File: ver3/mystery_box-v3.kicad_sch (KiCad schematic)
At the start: 3 parts, among them J1 Conn_01x02_Socket, Q1 IRLZ44N

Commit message: first draft v3
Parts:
- added D1, D2, D3: D, symbol Device:D
- added J2, J3, J4, J5: Conn_01x02_Socket, symbol Connector:Conn_01x02_Socket
- added Q2, Q3: IRLZ44N, Package_TO_SOT_THT:TO-220-3_Vertical, symbol Transistor_FET:IRLZ44N
- added R1, R2: R, symbol Device:R
- added U1: TXS0102DQE, Package_SON:X2SON-8_1.4x1mm_P0.35mm, symbol Logic_LevelTranslator:TXS0102DQE
- added U2: MAX485E, Package_SO:SOIC-8_3.9x4.9mm_P1.27mm, symbol Interface_UART:MAX485E
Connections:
- net GND: now also ESP32_S1. (14), Q2.3 (S), Q3.3 (S)
- net VCC 12V: now also D1.1 (K), D2.1 (K), D3.1 (K), J2.1 (Pin_1), J3.1 (Pin_1)
- net at J1.2 (Pin_2), Q1.2 (D): now also D1.2 (A)
- new net: D3.2 (A), J3.2 (Pin_2), Q3.2 (D)
- new net: J4.1 (Pin_1), R2.1
- new net: R2.2, U1.3 (A2)
- new net: J4.2 (Pin_2), R1.1
- new net: R1.2, U1.2 (A1)
- new net: ESP32_S1. (14), Q2.1 (G)
- new net: ESP32_S1. (14), Q3.1 (G)
- new net: ESP32_S1. (14), U1.6 (B2)
- new net: ESP32_S1. (14), U1.7 (B1)
- new net: ESP32_S1. (14), U2.3 (DE)
- new net: ESP32_S1. (14), U2.4 (DI)
- new net: D2.2 (A), J2.2 (Pin_2), Q2.2 (D)
- new net: J5.1 (Pin_1), U2.6 (A)
- new net: J5.2 (Pin_2), U2.7 (B)
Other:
- moved on the sheet: ESP32_S1, J1, Q1

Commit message: update 2. meeting
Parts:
- removed J1, J2, J3, J4, J5: Conn_01x02_Socket, symbol Connector:Conn_01x02_Socket
- removed U1: TXS0102DQE, Package_SON:X2SON-8_1.4x1mm_P0.35mm, symbol Logic_LevelTranslator:TXS0102DQE
- added F1, F2, F3, F4: Fuse, symbol Device:Fuse
- added J1, J10, J11, J12, J13, J14, J15, J16, J17, J2, J3, J4, J5, J7, J8, J9: Screw_Terminal_01x02, symbol Connector:Screw_Terminal_01x02
- added J18: RJ45 POE, symbol Connector:RJ45
- added J19: RJ45 IN, symbol Connector:RJ45
- added J6: Conn_01x02_Socket, symbol Connector:Conn_01x02_Socket
- added R10, R3, R6, R8: 100K, symbol Device:R
- added R4, R5, R7, R9: 330K, symbol Device:R
- added U1: ~, eigene_footprints:level_shifter, symbol eigene:levelshifter_2channel
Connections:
- net GND: now also U2.5 (GND), J10.1 (Pin_1), J11.1 (Pin_1), J12.1 (Pin_1), J13.1 (Pin_1), J14.1 (Pin_1), J15.1 (Pin_1), J16.1 (Pin_1), J17.1 (Pin_1), J18.7, J18.8, J6.1 (Pin_1), J7.1 (Pin_1), J8.1 (Pin_1), J9.1 (Pin_1), R10.1, R3.1, R6.1, R8.1, U1.10 (GND), U1.4 (GND)
- net VCC 12V: now also F1.2, F2.1, F3.1, F4.1, J18.4, J18.5, J6.2 (Pin_2), J7.2 (Pin_2); no longer D1.1 (K), D2.1 (K), D3.1 (K)
- net at D3.2 (A), Q3.2 (D): now also J2.2 (Pin_2)
- net at R2.1: now also J5.1 (Pin_1)
- net at R2.2: now also U1.7 (HV1)
- net at R1.1: now also J5.2 (Pin_2)
- net at R1.2: now also U1.11 (HV3)
- net at D1.2 (A), Q1.2 (D): now also J1.2 (Pin_2)
- net at D2.2 (A), Q2.2 (D): now also J3.2 (Pin_2)
- net at U2.6 (A): now also J4.1 (Pin_1)
- net at U2.7 (B): now also J4.2 (Pin_2)
- net VCC 5V: now reaches U2.8 (VCC)
- net VCC 5V: now also U1.9 (HV)
- new net: ESP32_S1. (14), R7.1, R8.2
- new net: D2.1 (K), F2.2, J3.1 (Pin_1), R7.2
- new net: ESP32_S1. (14), R10.2, R9.1
- new net: F1.1, J10.2 (Pin_2), J11.2 (Pin_2), J12.2 (Pin_2), J13.2 (Pin_2), J14.2 (Pin_2), J15.2 (Pin_2), J16.2 (Pin_2), J17.2 (Pin_2), J8.2 (Pin_2), J9.2 (Pin_2), R4.2
- new net: J18.1, J19.1
- new net: J18.2, J19.2
- new net: J18.3, J19.3
- new net: J18.6, J19.6
- new net: D1.1 (K), F4.2, J1.1 (Pin_1), R5.2
- new net: D3.1 (K), F3.2, J2.1 (Pin_1), R9.2
- new net: ESP32_S1. (14), R5.1, R6.2
- new net: ESP32_S1. (14), U1.1 (LV1)
- new net: ESP32_S1. (14), U1.5 (LV3)
- new net: ESP32_S1. (14), R3.2, R4.1
- new net VCC 3V3: U1.3 (LV)
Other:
- moved on the sheet: D1, D2, Q1, Q2, R1, R2, U2

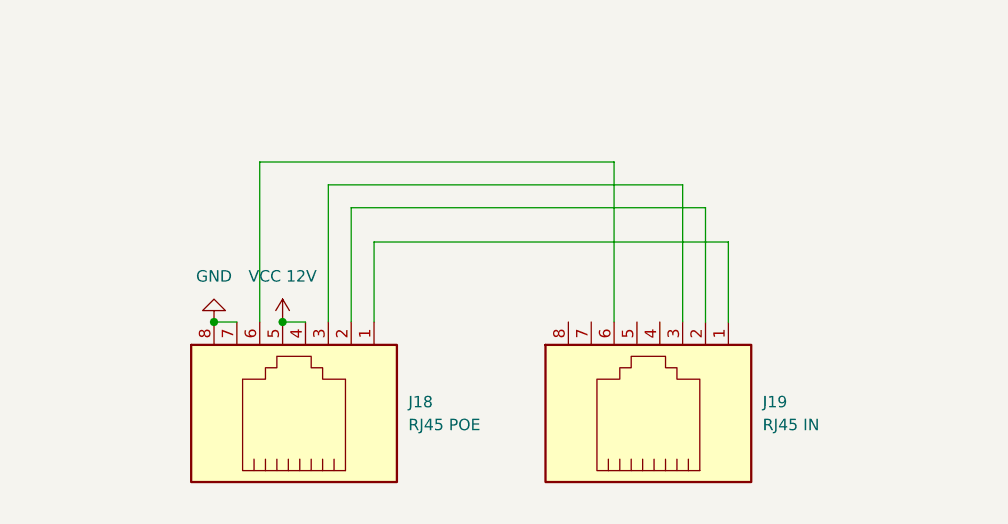
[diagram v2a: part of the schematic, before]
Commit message: added footprints for rj45, max485 module
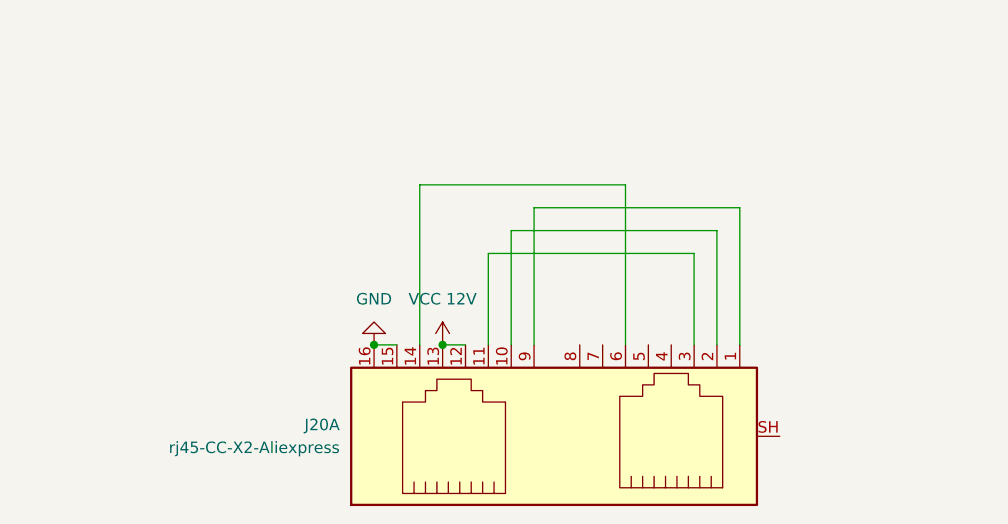
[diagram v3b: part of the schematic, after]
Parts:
- removed J18: RJ45 POE, symbol Connector:RJ45
- removed J19: RJ45 IN, symbol Connector:RJ45
- added J20: rj45-CC-X2-Aliexpress, eigene_footprints:RJ45_X2_CC_Aliexpress, symbol eigene:rj45-CC-X2-Aliexpress
- R1: footprint (none) -> Resistor_THT:R_Axial_DIN0207_L6.3mm_D2.5mm_P10.16mm_Horizontal
- U2: footprint Package_SO:SOIC-8_3.9x4.9mm_P1.27mm -> eigene_footprints:max845 modul
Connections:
- net GND: now also J20.15, J20.16
- net VCC 12V: now also J20.12, J20.13
- new net: J20.1, J20.9
- new net: J20.10, J20.2
- new net: J20.11, J20.3
- new net: J20.14, J20.6

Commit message: pcb editor beginning
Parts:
- removed ESP32_S1: ~, symbol waveshare_esp32_s3_mini_zero:Waveshare_ESP32_S3_Mini_Zero
- removed J4: Screw_Terminal_01x02, symbol Connector:Screw_Terminal_01x02
- removed J6: Conn_01x02_Socket, symbol Connector:Conn_01x02_Socket
- added ESP32_S1: ~, eigene_footprints:ESP32-S3-Zero, symbol eigene:Waveshare_ESP32_S3_Mini_Zero
- added J18: Barrel_Jack_MountingPin, eigene_footprints:CUI_PJ-050BH, symbol Connector:Barrel_Jack_MountingPin
- added dmx_out1: DMX Out, TerminalBlock:TerminalBlock_MaiXu_MX126-5.0-03P_1x03_P5.00mm, symbol Connector:Screw_Terminal_01x03
- 12v_input_terminal1: renamed from J7; footprint (none) -> TerminalBlock:TerminalBlock_MaiXu_MX126-5.0-02P_1x02_P5.00mm
- D1, D2, D3: footprint (none) -> Diode_THT:D_DO-15_P10.16mm_Horizontal
- F1, F2, F3, F4: footprint (none) -> eigene_footprints:FUSE SPACIGER SPACER
- J10, J11, J12, J13, J14, J15, J16, J17, J8, J9: footprint (none) -> TerminalBlock:TerminalBlock_MaiXu_MX126-5.0-02P_1x02_P5.00mm
- R10, R2, R3, R4, R5, R6, R7, R8, R9: footprint (none) -> Resistor_THT:R_Axial_DIN0207_L6.3mm_D2.5mm_P10.16mm_Horizontal
- neopixel_out1: renamed from J5; footprint (none) -> TerminalBlock:TerminalBlock_MaiXu_MX126-5.0-02P_1x02_P5.00mm
- switched_output_01: renamed from J3; footprint (none) -> TerminalBlock:TerminalBlock_MaiXu_MX126-5.0-02P_1x02_P5.00mm
- switched_output_02: renamed from J1; footprint (none) -> TerminalBlock:TerminalBlock_MaiXu_MX126-5.0-02P_1x02_P5.00mm
- switched_output_03: renamed from J2; footprint (none) -> TerminalBlock:TerminalBlock_MaiXu_MX126-5.0-02P_1x02_P5.00mm
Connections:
- net GND: now also ESP32_S1. (7), J18.2, dmx_out1.1 (Pin_1)
- net VCC 12V: now also J18.1
- net at R7.1, R8.2: now also ESP32_S1. (7)
- net at R2.1: now also neopixel_out1.2 (Pin_2); no longer neopixel_out1.1 (Pin_1)
- net at R10.2, R9.1: now also ESP32_S1. (7)
- net at R1.1: now also neopixel_out1.1 (Pin_1); no longer neopixel_out1.2 (Pin_2)
- net at Q1.1 (G): now also ESP32_S1. (7)
- net at Q2.1 (G): now also ESP32_S1. (7)
- net at R5.1, R6.2: now also ESP32_S1. (7)
- net at Q3.1 (G): now also ESP32_S1. (7)
- net at U1.1 (LV1): now also ESP32_S1. (7)
- net at U1.5 (LV3): now also ESP32_S1. (7)
- net at R3.2, R4.1: now also ESP32_S1. (7)
- net at U2.3 (DE): now also ESP32_S1. (7)
- net at U2.4 (DI): now also ESP32_S1. (7)
- net at U2.6 (A): now also dmx_out1.2 (Pin_2)
- net at U2.7 (B): now also dmx_out1.3 (Pin_3)
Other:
- moved on the sheet: neopixel_out1

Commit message: smart switch
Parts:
- removed F1, F2, F3, F4: Fuse, eigene_footprints:FUSE SPACIGER SPACER, symbol Device:Fuse
- removed R10, R6, R8: 100K, Resistor_THT:R_Axial_DIN0207_L6.3mm_D2.5mm_P10.16mm_Horizontal, symbol Device:R
- removed R4, R5, R7, R9: 330K, Resistor_THT:R_Axial_DIN0207_L6.3mm_D2.5mm_P10.16mm_Horizontal, symbol Device:R
- added U3: ~, Package_SO:SOIC-8_3.9x4.9mm_P1.27mm, symbol eigene:BV1HD090FJ-C
- R3: value 100K -> R100K
- renumbered ESP32_S1 to ESP32_S3
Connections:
- net GND: now also U3.3 (GND); no longer R3.1
- net VCC 12V: now also J15.2 (Pin_2), J16.2 (Pin_2), J17.2 (Pin_2)
- net VCC 3V3: now also R3.1
- net at D2.1 (K), switched_output_01.1 (Pin_1): now also D1.1 (K), D3.1 (K), J10.2 (Pin_2), J11.2 (Pin_2), J12.2 (Pin_2), J13.2 (Pin_2), J14.2 (Pin_2), J8.2 (Pin_2), J9.2 (Pin_2), switched_output_02.1 (Pin_1), switched_output_03.1 (Pin_1), U3.4 (OUT)
- net at ESP32_S3. (7), R3.2: now also U3.2 (ST)
- new net: ESP32_S3. (7), U3.1 (IN)
- new net VCC: U3.5 (VBB), U3.6 (VBB), U3.7 (VBB), U3.8 (VBB)

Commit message: final prototype v3
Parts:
- added J1, J2, J3, J4: Conn_01x02_Pin, Connector_PinHeader_1.00mm:PinHeader_1x02_P1.00mm_Vertical, symbol Connector:Conn_01x02_Pin
- added neopixel_pwr1: Screw_Terminal_01x02, TerminalBlock:TerminalBlock_MaiXu_MX126-5.0-02P_1x02_P5.00mm, symbol Connector:Screw_Terminal_01x02
- R3: value R100K -> R
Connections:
- net VCC is gone; now on net VCC 12V: U3.5 (VBB), U3.6 (VBB), U3.7 (VBB), U3.8 (VBB)
- net GND: now also ESP32_S3.GND, J4.2 (Pin_2), neopixel_pwr1.1 (Pin_1); no longer ESP32_S3. (7)
- net at Q1.1 (G): now also ESP32_S3.8; no longer ESP32_S3. (7)
- net at Q2.1 (G): now also ESP32_S3.7; no longer ESP32_S3. (7)
- net at Q3.1 (G): now also ESP32_S3.9; no longer ESP32_S3. (7)
- net at U3.1 (IN): now also ESP32_S3.11; no longer ESP32_S3. (7)
- net at R3.2, U3.2 (ST): now also ESP32_S3.10; no longer ESP32_S3. (7)
- net at U1.1 (LV1): now also ESP32_S3.6; no longer ESP32_S3. (7)
- net at U1.5 (LV3): now also ESP32_S3.5; no longer ESP32_S3. (7)
- net at U2.3 (DE): now also ESP32_S3.4; no longer ESP32_S3. (7)
- net at U2.4 (DI): now also ESP32_S3.3; no longer ESP32_S3. (7)
- net SW 12V: now reaches D1.1 (K), D2.1 (K), D3.1 (K), J10.2 (Pin_2), J11.2 (Pin_2), J12.2 (Pin_2), J13.2 (Pin_2), J14.2 (Pin_2), J8.2 (Pin_2), J9.2 (Pin_2), U3.4 (OUT), switched_output_01.1 (Pin_1), switched_output_02.1 (Pin_1), switched_output_03.1 (Pin_1)
- net SW 12V: now also neopixel_pwr1.2 (Pin_2)
- new net: ESP32_S3.1, J2.1 (Pin_1)
- new net: ESP32_S3.12, J1.1 (Pin_1)
- new net: ESP32_S3.13, J1.2 (Pin_2)
- new net: ESP32_S3.2, J2.2 (Pin_2)
- new net: ESP32_S3.5V, J4.1 (Pin_1)
- new net: ESP32_S3.RX, J3.1 (Pin_1)
- new net: ESP32_S3.TX, J3.2 (Pin_2)

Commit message: first edit of serious ver3
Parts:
- removed 12v_input_terminal1, neopixel_out1, neopixel_pwr1: Screw_Terminal_01x02, TerminalBlock:TerminalBlock_MaiXu_MX126-5.0-02P_1x02_P5.00mm, symbol Connector:Screw_Terminal_01x02
- removed J1, J2, J3, J4: Conn_01x02_Pin, Connector_PinHeader_1.00mm:PinHeader_1x02_P1.00mm_Vertical, symbol Connector:Conn_01x02_Pin
- removed U1: ~, eigene_footprints:level_shifter, symbol eigene:levelshifter_2channel
- removed U2: MAX485E, eigene_footprints:max845 modul, symbol Interface_UART:MAX485E
- removed dmx_out1: DMX Out, TerminalBlock:TerminalBlock_MaiXu_MX126-5.0-03P_1x03_P5.00mm, symbol Connector:Screw_Terminal_01x03
- added D4: 1N914, Diode_THT:D_DO-35_SOD27_P7.62mm_Horizontal, symbol Diode:1N914
- added GPIO13_SERIAL, JMP_NEO1_PWR, JMP_NEO2_PWR, JMP_NEO3_PWR: Conn_01x03_Pin, symbol Connector:Conn_01x03_Pin
- added GPIO_CONN: Conn_01x04_Pin, symbol Connector:Conn_01x04_Pin
- added GPIO_T1, GPIO_T2, GPIO_T3, J1: Screw_Terminal_01x02, TerminalBlock:TerminalBlock_MaiXu_MX126-5.0-02P_1x02_P5.00mm, symbol Connector:Screw_Terminal_01x02
- added JMP_5V_USB-BUCK: Conn_01x02_Pin, symbol Connector:Conn_01x02_Pin
- added NEOPIXEL1, NEOPIXEL2, NEOPIXEL3: WS2812B, LED_SMD:LED_WS2812B_PLCC4_5.0x5.0mm_P3.2mm, symbol LED:WS2812B
- added NEO_T1, NEO_T2, NEO_T3: Screw_Terminal_01x03, symbol Connector:Screw_Terminal_01x03
- added R4, R5: R, symbol Device:R
- R1, R2: footprint Resistor_THT:R_Axial_DIN0207_L6.3mm_D2.5mm_P10.16mm_Horizontal -> (none)
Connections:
- net GND: now also GPIO_T1.2 (Pin_2), GPIO_T3.1 (Pin_1), J1.1 (Pin_1), NEOPIXEL1.3 (VSS), NEOPIXEL2.3 (VSS), NEOPIXEL3.3 (VSS), NEO_T1.3 (Pin_3), NEO_T2.3 (Pin_3), NEO_T3.3 (Pin_3)
- net VCC 3V3: now also ESP32_S3.3V3 (3.3V(OUT))
- net at R2.1: now also GPIO_CONN.2 (Pin_2), GPIO_T2.2 (Pin_2)
- net at R2.2: now also ESP32_S3.2
- net at ESP32_S3.1: now also R1.2
- net at R3.2, U3.2 (ST): now also ESP32_S3.11; no longer ESP32_S3.10
- net at U3.1 (IN): now also ESP32_S3.12; no longer ESP32_S3.11
- net at ESP32_S3.13: now also GPIO13_SERIAL.1 (Pin_1)
- net at ESP32_S3.3: now also R4.2
- net at ESP32_S3.4: now also R5.2
- net at ESP32_S3.5: now also NEOPIXEL1.4 (DIN)
- net VCC 5V USB: now reaches ESP32_S3.5V
- net VCC 5V USB: now also D4.2 (A), JMP_5V_USB-BUCK.1 (Pin_1)
- net at ESP32_S3.6: now also NEOPIXEL2.4 (DIN)
- net at ESP32_S3.7: now also NEOPIXEL3.4 (DIN); no longer Q2.1 (G)
- net at ESP32_S3.8: now also Q2.1 (G); no longer Q1.1 (G)
- net at Q3.1 (G): now also ESP32_S3.10; no longer ESP32_S3.9
- net at ESP32_S3.RX: now also GPIO13_SERIAL.2 (Pin_2)
- net at ESP32_S3.TX: now also GPIO13_SERIAL.3 (Pin_3)
- net at R1.1: now also GPIO_CONN.1 (Pin_1), GPIO_T1.1 (Pin_1)
- net SW 12V renamed VCC 12V SW
- net VCC 12V SW: now also J1.2 (Pin_2), JMP_NEO1_PWR.1 (Pin_1), JMP_NEO2_PWR.1 (Pin_1), JMP_NEO3_PWR.1 (Pin_1)
- new net: JMP_NEO3_PWR.2 (Pin_2), NEO_T3.1 (Pin_1)
- new net: JMP_NEO1_PWR.2 (Pin_2), NEO_T1.1 (Pin_1)
- new net: D4.1 (K), NEOPIXEL1.1 (VDD), NEOPIXEL2.1 (VDD), NEOPIXEL3.1 (VDD)
- new net: ESP32_S3.9, Q1.1 (G)
- new net: GPIO_CONN.3 (Pin_3), GPIO_T2.1 (Pin_1), R4.1
- new net: JMP_NEO2_PWR.2 (Pin_2), NEO_T2.1 (Pin_1)
- new net: NEOPIXEL2.2 (DOUT), NEO_T2.2 (Pin_2)
- new net: GPIO_CONN.4 (Pin_4), GPIO_T3.2 (Pin_2), R5.1
- new net: NEOPIXEL3.2 (DOUT), NEO_T3.2 (Pin_2)
- new net: NEOPIXEL1.2 (DOUT), NEO_T1.2 (Pin_2)
- new net VCC 5V BUCK: JMP_5V_USB-BUCK.2 (Pin_2), JMP_NEO1_PWR.3 (Pin_3), JMP_NEO2_PWR.3 (Pin_3), JMP_NEO3_PWR.3 (Pin_3)
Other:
- moved on the sheet: D1, D2, D3, ESP32_S3, J15, J16, J17, J18, J20A, Q1, Q2, Q3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

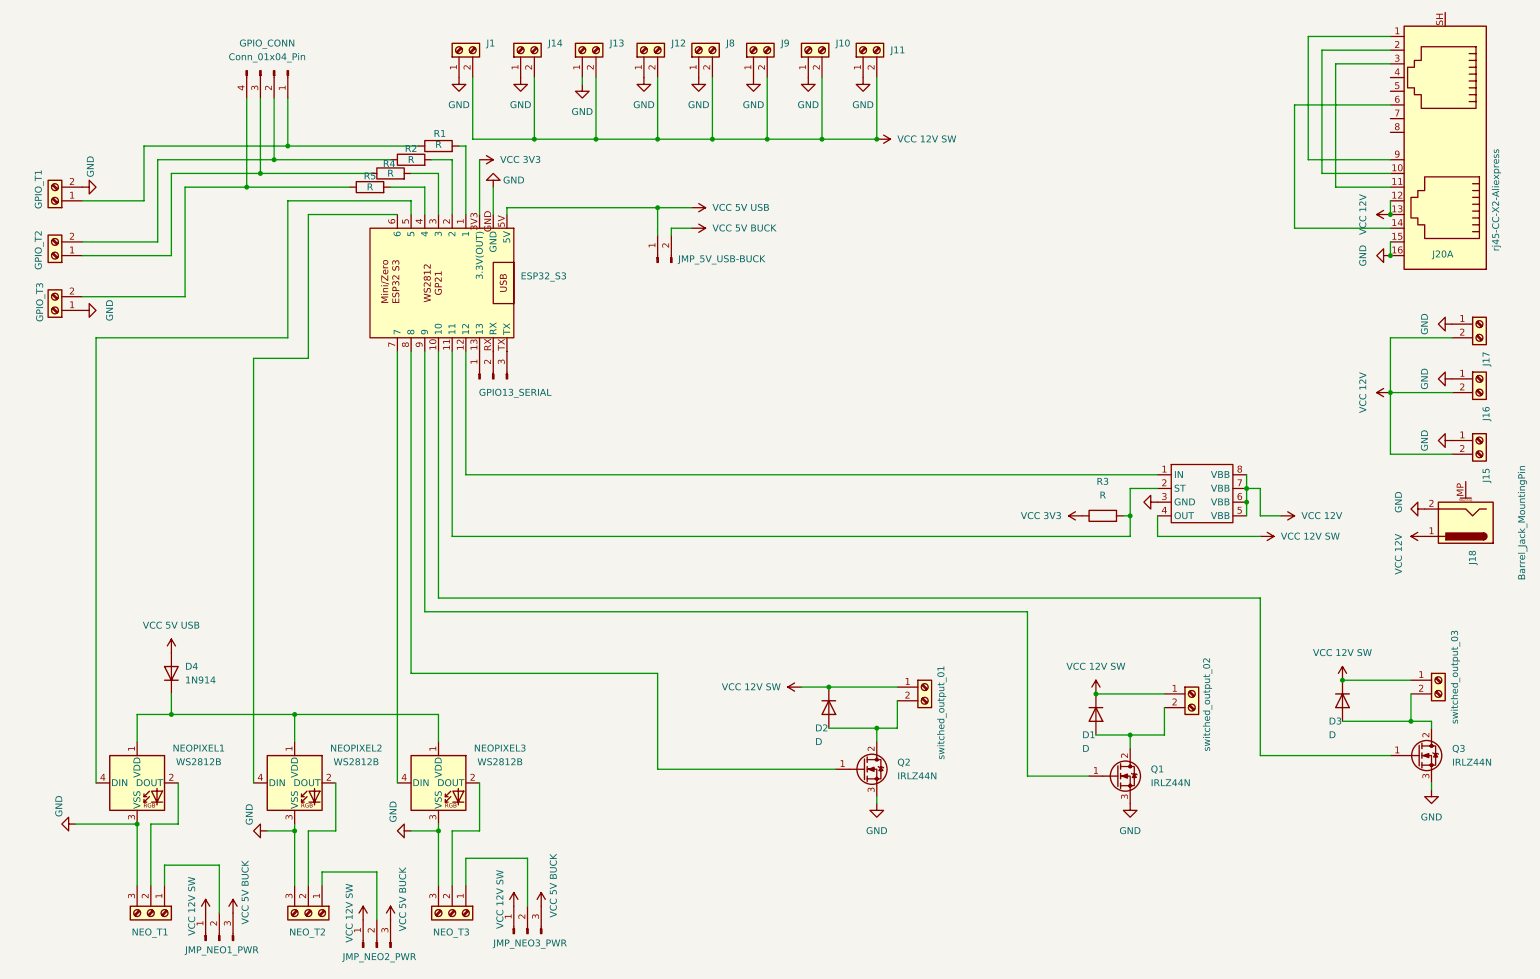
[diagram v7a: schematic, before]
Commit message: schematic with converter + footprints
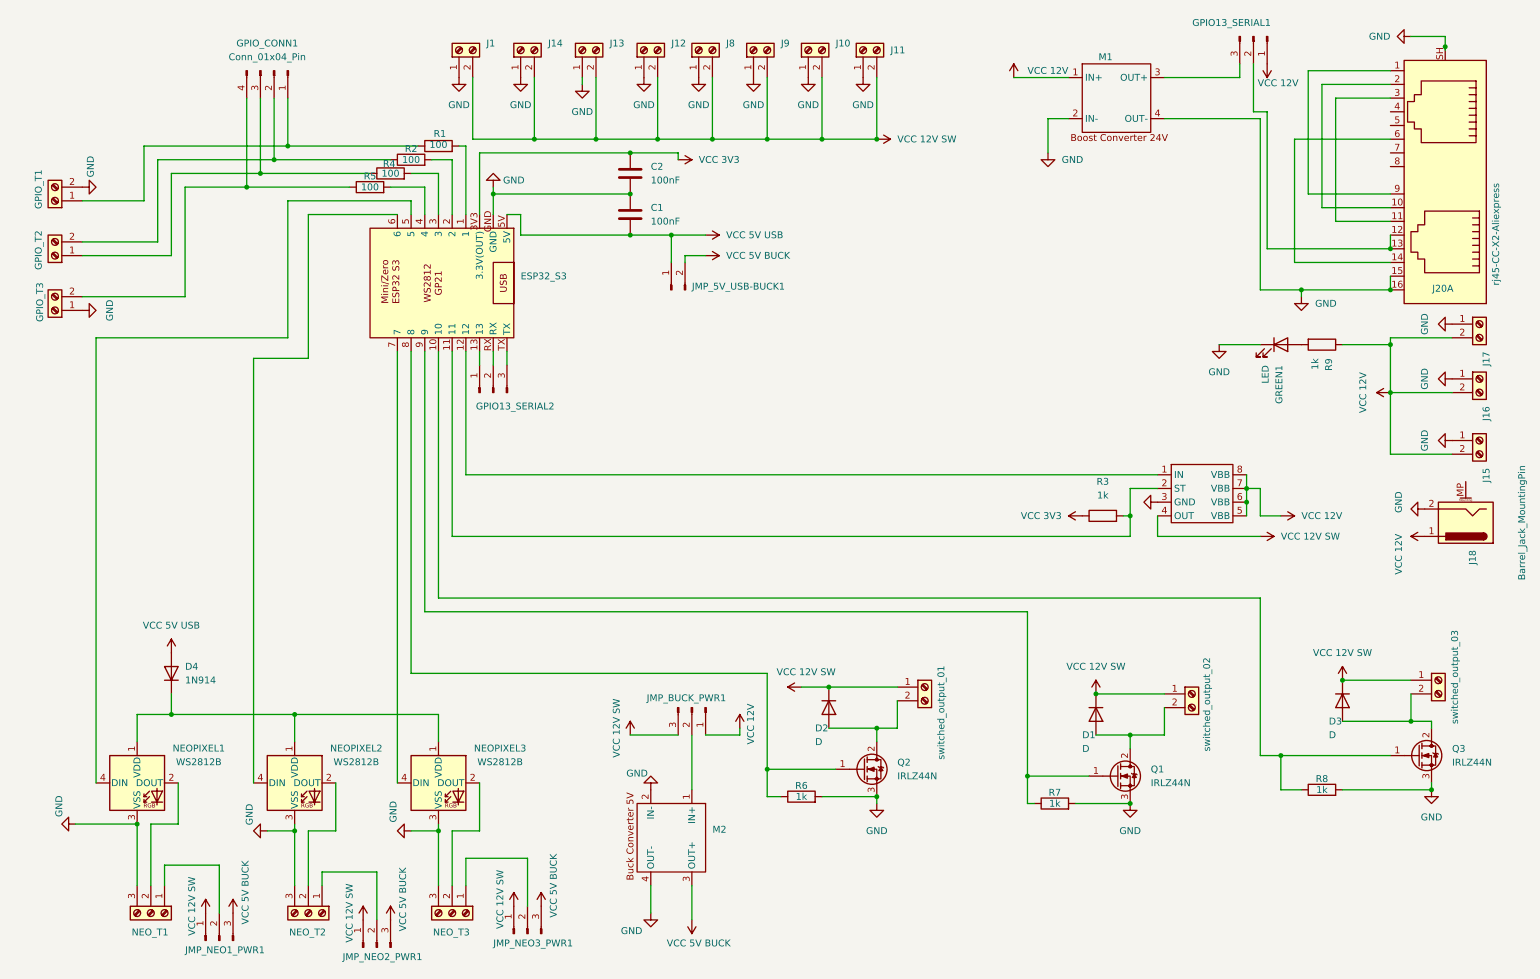
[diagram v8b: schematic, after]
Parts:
- added C1, C2: 100nF, Capacitor_THT:C_Rect_L7.0mm_W2.5mm_P5.00mm, symbol Device:C
- added GPIO13_SERIAL1, JMP_BUCK_PWR1: Conn_01x03_Pin, symbol Connector:Conn_01x03_Pin
- added GREEN1: LED, LED_THT:LED_D3.0mm_Horizontal_O1.27mm_Z2.0mm_Clear, symbol Device:LED
- added M1: ~, symbol eigene:Boost-Converter-24V
- added M2: ~, symbol eigene:Buck-Converter-5V
- added R6, R7, R8, R9: 1k, Resistor_THT:R_Axial_DIN0207_L6.3mm_D2.5mm_P10.16mm_Horizontal, symbol Device:R
- R1, R2, R4, R5: value R -> 100; footprint (none) -> Resistor_THT:R_Axial_DIN0207_L6.3mm_D2.5mm_P10.16mm_Horizontal
- R3: value R -> 1k
- renumbered GPIO13_SERIAL to GPIO13_SERIAL2, GPIO_CONN to GPIO_CONN1, JMP_5V_USB-BUCK to JMP_5V_USB-BUCK1, JMP_NEO1_PWR to JMP_NEO1_PWR1, JMP_NEO2_PWR to JMP_NEO2_PWR1, JMP_NEO3_PWR to JMP_NEO3_PWR1
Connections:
- net GND: now also J20.SH, C1.1, C2.2, GREEN1.1 (K), M1.2 (IN-), M1.4 (OUT-), M2.2 (IN-), M2.4 (OUT-), R6.2, R7.2, R8.2
- net VCC 12V: now also GPIO13_SERIAL1.1 (Pin_1), JMP_BUCK_PWR1.1 (Pin_1), M1.1 (IN+), R9.1; no longer J20.12, J20.13
- net VCC 12V SW: now also JMP_BUCK_PWR1.3 (Pin_3)
- net VCC 3V3: now also C2.1
- net VCC 5V BUCK: now also M2.3 (OUT+)
- net VCC 5V USB: now also C1.2
- net at ESP32_S3.10, Q3.1 (G): now also R8.1
- net at ESP32_S3.8, Q2.1 (G): now also R6.1
- net at ESP32_S3.9, Q1.1 (G): now also R7.1
- new net: GPIO13_SERIAL1.2 (Pin_2), J20.12, J20.13
- new net: GPIO13_SERIAL1.3 (Pin_3), M1.3 (OUT+)
- new net: JMP_BUCK_PWR1.2 (Pin_2), M2.1 (IN+)
- new net: GREEN1.2 (A), R9.2
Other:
- title: (none) -> mystery box
- moved on the sheet: GPIO13_SERIAL2, J20A, JMP_5V_USB-BUCK1
